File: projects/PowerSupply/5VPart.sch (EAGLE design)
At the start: 10 parts, among them IC1 LM2596T, SW1 LSP10

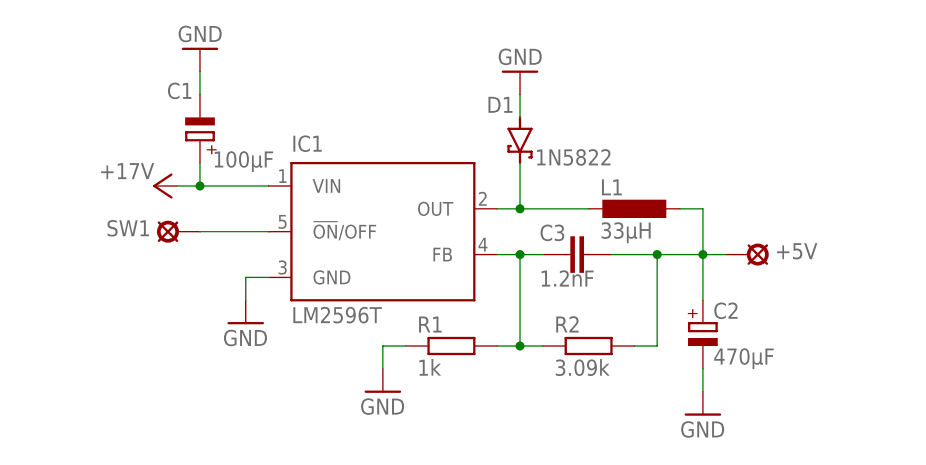
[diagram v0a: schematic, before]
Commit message: feat: power supply
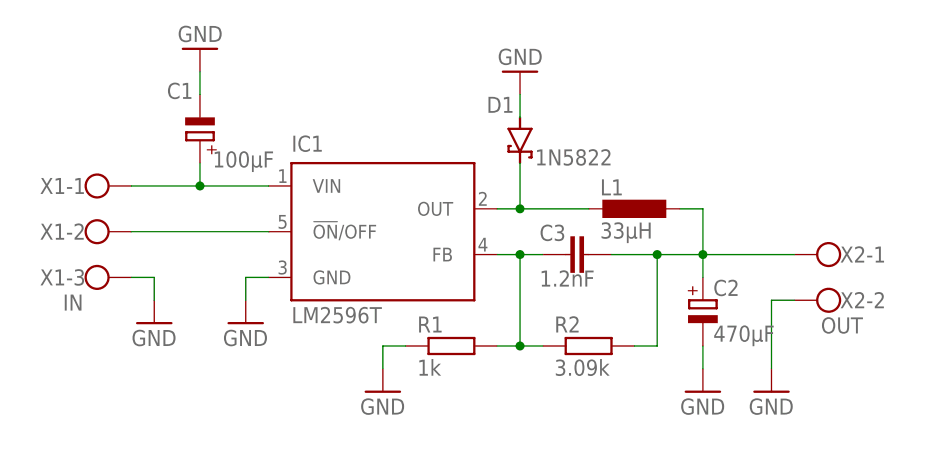
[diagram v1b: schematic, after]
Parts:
- removed +5V, SW1: LSP10, solpad:LSP10
- added X1: IN, con-wago-500:W237-103
- added X2: OUT, con-wago-500:W237-102
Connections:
- removed net VCC: C1.+, IC1.VIN
- new net N$5: C1.+, IC1.VIN, X1-1.KL
- net GND: now also X1-3.KL, X2-2.KL
- net N$2: now also X1-2.KL; no longer SW1.MP
- net N$3: now also X2-1.KL; no longer +5V.MP
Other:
- moved on the sheet: C2
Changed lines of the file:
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@@
 <part name="C1" library="rcl" library_urn="urn:adsk.eagle:library:334" deviceset="CPOL-EU" device="E2.5-6" package3d_urn="urn:adsk.eagle:package:23349/1" value="100µF"/>
 <part name="GND2" library="supply1" library_urn="urn:adsk.eagle:library:371" deviceset="GND" device=""/>
-<part name="P+1" library="supply1" library_urn="urn:adsk.eagle:library:371" deviceset="VCC" device="" value="+17V"/>
 <part name="C2" library="rcl" library_urn="urn:adsk.eagle:library:334" deviceset="CPOL-EU" device="E2.5-6" package3d_urn="urn:adsk.eagle:package:23349/1" value="470µF"/>
 <part name="D1" library="diode" library_urn="urn:adsk.eagle:library:210" deviceset="SCHOTTKY-DIODE" device="C4111-15" package3d_urn="urn:adsk.eagle:package:43355/2" value="1N5822"/>
 <part name="GND3" library="supply1" library_urn="urn:adsk.eagle:library:371" deviceset="GND" device=""/>
 <part name="GND4" library="supply1" library_urn="urn:adsk.eagle:library:371" deviceset="GND" device=""/>
-<part name="SW1" library="solpad" library_urn="urn:adsk.eagle:library:364" deviceset="LSP10" device="" package3d_urn="urn:adsk.eagle:package:26501/1"/>
 <part name="R1" library="rcl" library_urn="urn:adsk.eagle:library:334" deviceset="R-EU_" device="0207/10" package3d_urn="urn:adsk.eagle:package:23491/2" value="1k"/>
 <part name="R2" library="rcl" library_urn="urn:adsk.eagle:library:334" deviceset="R-EU_" device="0207/10" package3d_urn="urn:adsk.eagle:package:23491/2" value="3.09k"/>
@@
 <part name="GND5" library="supply1" library_urn="urn:adsk.eagle:library:371" deviceset="GND" device=""/>
 <part name="L1" library="rcl" library_urn="urn:adsk.eagle:library:334" deviceset="L-EU" device="TJ3-U2" package3d_urn="urn:adsk.eagle:package:23497/1" value="33µH"/>
-<part name="+5V" library="solpad" library_urn="urn:adsk.eagle:library:364" deviceset="LSP10" device="" package3d_urn="urn:adsk.eagle:package:26501/1"/>
+<part name="X1" library="con-wago-500" library_urn="urn:adsk.eagle:library:195" deviceset="W237-103" device="" package3d_urn="urn:adsk.eagle:package:10691/1" value="IN"/>
+<part name="X2" library="con-wago-500" library_urn="urn:adsk.eagle:library:195" deviceset="W237-102" device="" package3d_urn="urn:adsk.eagle:package:10688/1" value="OUT"/>
+<part name="GND6" library="supply1" library_urn="urn:adsk.eagle:library:371" deviceset="GND" device=""/>
+<part name="GND8" library="supply1" library_urn="urn:adsk.eagle:library:371" deviceset="GND" device=""/>
 </parts>
 <sheets>
@@
 <attribute name="VALUE" x="35.56" y="93.98" size="1.778" layer="96" rot="R180"/>
 </instance>
-<instance part="P+1" gate="VCC" x="27.94" y="76.2" smashed="yes" rot="R90">
-<attribute name="VALUE" x="27.94" y="78.74" size="1.778" layer="96" rot="R180"/>
-</instance>
-<instance part="C2" gate="G$1" x="88.9" y="60.96" smashed="yes">
-<attribute name="NAME" x="90.043" y="61.4426" size="1.778" layer="95"/>
-<attribute name="VALUE" x="90.043" y="56.3626" size="1.778" layer="96"/>
+<instance part="C2" gate="G$1" x="88.9" y="63.5" smashed="yes">
+<attribute name="NAME" x="90.043" y="63.9826" size="1.778" layer="95"/>
+<attribute name="VALUE" x="90.043" y="58.9026" size="1.778" layer="96"/>
 </instance>
 <instance part="D1" gate="G$1" x="68.58" y="81.28" smashed="yes" rot="R270">
@@
 <attribute name="VALUE" x="71.12" y="91.44" size="1.778" layer="96" rot="R180"/>
 </instance>
-<instance part="GND4" gate="1" x="88.9" y="50.8" smashed="yes">
-<attribute name="VALUE" x="86.36" y="48.26" size="1.778" layer="96"/>
-</instance>
-<instance part="SW1" gate="1" x="30.48" y="71.12" smashed="yes" rot="R90">
-<attribute name="NAME" x="27.559" y="72.39" size="1.778" layer="95" rot="R180"/>
+<instance part="GND4" gate="1" x="88.9" y="53.34" smashed="yes">
+<attribute name="VALUE" x="86.36" y="50.8" size="1.778" layer="96"/>
 </instance>
 <instance part="R1" gate="G$1" x="60.96" y="58.42" smashed="yes">
@@
 <attribute name="VALUE" x="77.47" y="70.358" size="1.778" layer="96"/>
 </instance>
-<instance part="+5V" gate="1" x="93.98" y="68.58" smashed="yes" rot="MR90">
-<attribute name="NAME" x="96.901" y="69.85" size="1.778" layer="95" rot="MR180"/>
+<instance part="X1" gate="-1" x="20.32" y="76.2" smashed="yes">
+<attribute name="NAME" x="20.32" y="77.089" size="1.778" layer="95" rot="R180"/>
+</instance>
+<instance part="X1" gate="-2" x="20.32" y="71.12" smashed="yes">
+<attribute name="NAME" x="20.32" y="72.009" size="1.778" layer="95" rot="R180"/>
+</instance>
+<instance part="X1" gate="-3" x="20.32" y="66.04" smashed="yes">
+<attribute name="VALUE" x="17.78" y="62.357" size="1.778" layer="96"/>
+<attribute name="NAME" x="20.32" y="66.929" size="1.778" layer="95" rot="R180"/>
+</instance>
+<instance part="X2" gate="-1" x="104.14" y="68.58" smashed="yes" rot="MR0">
+<attribute name="NAME" x="104.14" y="69.469" size="1.778" layer="95" rot="MR180"/>
+</instance>
+<instance part="X2" gate="-2" x="104.14" y="63.5" smashed="yes" rot="MR0">
+<attribute name="VALUE" x="106.68" y="59.817" size="1.778" layer="96" rot="MR0"/>
+<attribute name="NAME" x="104.14" y="64.389" size="1.778" layer="95" rot="MR180"/>
+</instance>
+<instance part="GND6" gate="1" x="27.94" y="60.96" smashed="yes">
+<attribute name="VALUE" x="25.4" y="58.42" size="1.778" layer="96"/>
+</instance>
+<instance part="GND8" gate="1" x="96.52" y="53.34" smashed="yes">
+<attribute name="VALUE" x="93.98" y="50.8" size="1.778" layer="96"/>
 </instance>
 </instances>
@@
 <pinref part="GND4" gate="1" pin="GND"/>
 <pinref part="C2" gate="G$1" pin="-"/>
-<wire x1="88.9" y1="53.34" x2="88.9" y2="55.88" width="0.1524" layer="91"/>
+<wire x1="88.9" y1="55.88" x2="88.9" y2="58.42" width="0.1524" layer="91"/>
 </segment>
 <segment>
@@
 <wire x1="33.02" y1="86.36" x2="33.02" y2="88.9" width="0.1524" layer="91"/>
 </segment>
-</net>
-<net name="VCC" class="0">
 <segment>
-<pinref part="IC1" gate="G$1" pin="VIN"/>
-<pinref part="P+1" gate="VCC" pin="VCC"/>
-<wire x1="30.48" y1="76.2" x2="33.02" y2="76.2" width="0.1524" layer="91"/>
-<pinref part="C1" gate="G$1" pin="+"/>
-<wire x1="33.02" y1="76.2" x2="40.64" y2="76.2" width="0.1524" layer="91"/>
-<wire x1="33.02" y1="78.74" x2="33.02" y2="76.2" width="0.1524" layer="91"/>
-<junction x="33.02" y="76.2"/>
+<pinref part="X1" gate="-3" pin="KL"/>
+<pinref part="GND6" gate="1" pin="GND"/>
+<wire x1="25.4" y1="66.04" x2="27.94" y2="66.04" width="0.1524" layer="91"/>
+<wire x1="27.94" y1="66.04" x2="27.94" y2="63.5" width="0.1524" layer="91"/>
 </segment>
-</net>
-<net name="N$2" class="0">
 <segment>
-<pinref part="IC1" gate="G$1" pin="!ON!/OFF"/>
-<pinref part="SW1" gate="1" pin="MP"/>
-<wire x1="40.64" y1="71.12" x2="33.02" y2="71.12" width="0.1524" layer="91"/>
+<pinref part="X2" gate="-2" pin="KL"/>
+<wire x1="99.06" y1="63.5" x2="96.52" y2="63.5" width="0.1524" layer="91"/>
+<pinref part="GND8" gate="1" pin="GND"/>
+<wire x1="96.52" y1="63.5" x2="96.52" y2="55.88" width="0.1524" layer="91"/>
 </segment>
 </net>
@@
 <pinref part="C2" gate="G$1" pin="+"/>
 <wire x1="88.9" y1="73.66" x2="88.9" y2="68.58" width="0.1524" layer="91"/>
-<wire x1="88.9" y1="68.58" x2="88.9" y2="63.5" width="0.1524" layer="91"/>
+<wire x1="88.9" y1="68.58" x2="88.9" y2="66.04" width="0.1524" layer="91"/>
 <wire x1="83.82" y1="68.58" x2="88.9" y2="68.58" width="0.1524" layer="91"/>
 <junction x="83.82" y="68.58"/>
 <junction x="88.9" y="68.58"/>
-<pinref part="+5V" gate="1" pin="MP"/>
-<wire x1="91.44" y1="68.58" x2="88.9" y2="68.58" width="0.1524" layer="91"/>
+<pinref part="X2" gate="-1" pin="KL"/>
+<wire x1="99.06" y1="68.58" x2="88.9" y2="68.58" width="0.1524" layer="91"/>
 </segment>
 </net>
+<net name="N$2" class="0">
+<segment>
+<pinref part="IC1" gate="G$1" pin="!ON!/OFF"/>
+<pinref part="X1" gate="-2" pin="KL"/>
+<wire x1="40.64" y1="71.12" x2="25.4" y2="71.12" width="0.1524" layer="91"/>
+</segment>
+</net>
+<net name="N$5" class="0">
+<segment>
+<pinref part="X1" gate="-1" pin="KL"/>
+<pinref part="IC1" gate="G$1" pin="VIN"/>
+<wire x1="25.4" y1="76.2" x2="33.02" y2="76.2" width="0.1524" layer="91"/>
+<pinref part="C1" gate="G$1" pin="+"/>
+<wire x1="33.02" y1="76.2" x2="40.64" y2="76.2" width="0.1524" layer="91"/>
+<wire x1="33.02" y1="78.74" x2="33.02" y2="76.2" width="0.1524" layer="91"/>
+<junction x="33.02" y="76.2"/>
+</segment>
+</net>

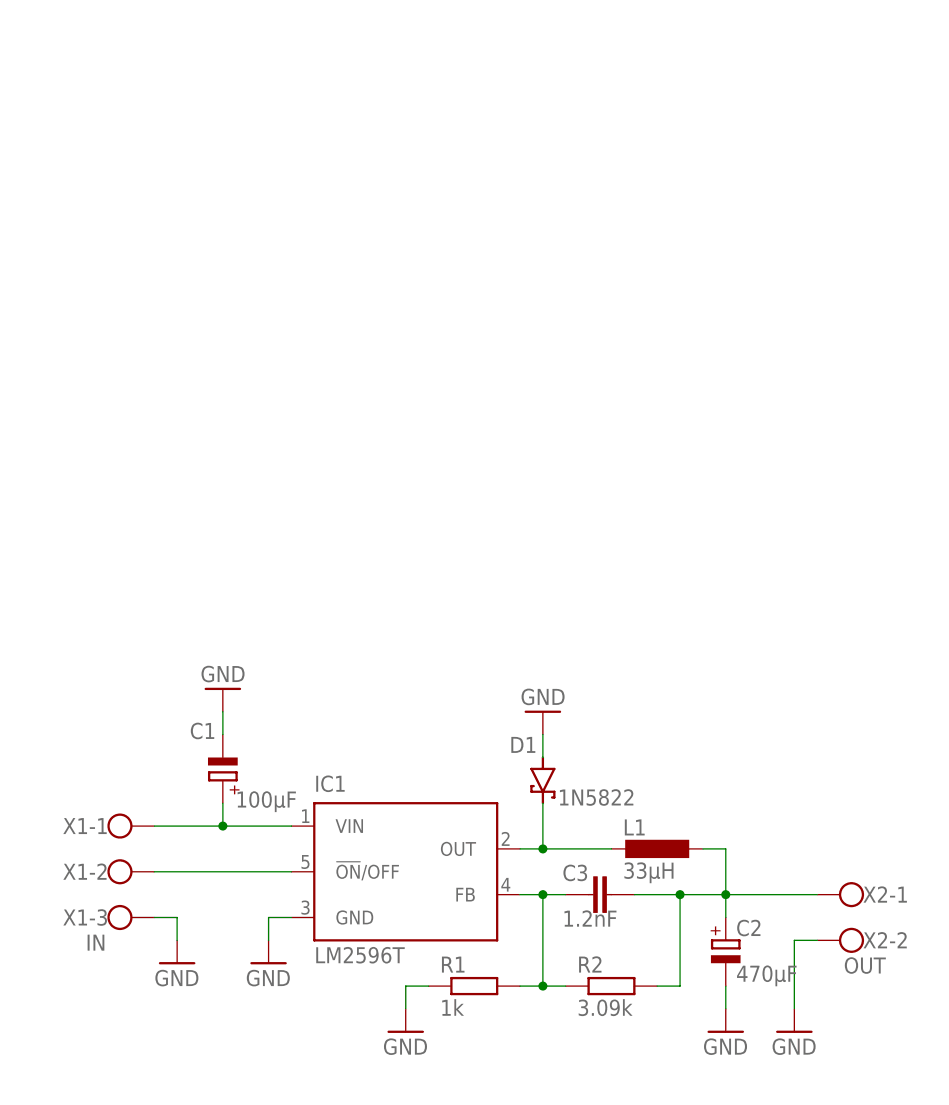
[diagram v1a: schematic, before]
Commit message: feat: power supply
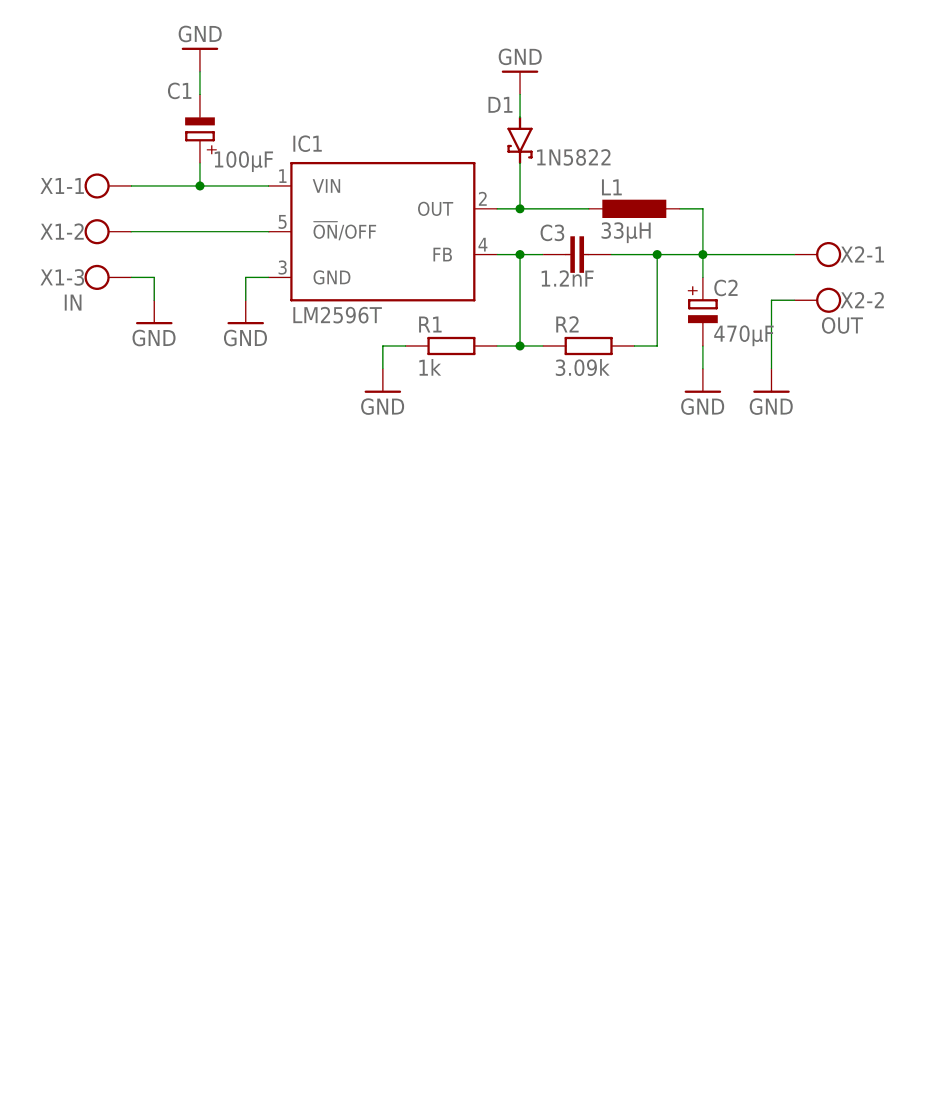
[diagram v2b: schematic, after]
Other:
- moved on the sheet: C1, C2, C3, D1, IC1, L1, R1, R2, X1-1, X1-2, X1-3, X2-1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
